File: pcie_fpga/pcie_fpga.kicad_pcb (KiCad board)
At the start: 4 copper layers, 50 x 70 mm, 18 parts, among them J3 Bus_PCI_Express_x4, U1 XC7A50T-FGG484, U2 LTC6957xMS-2, X1 ECS-2520MVQ-1000-BN-TR

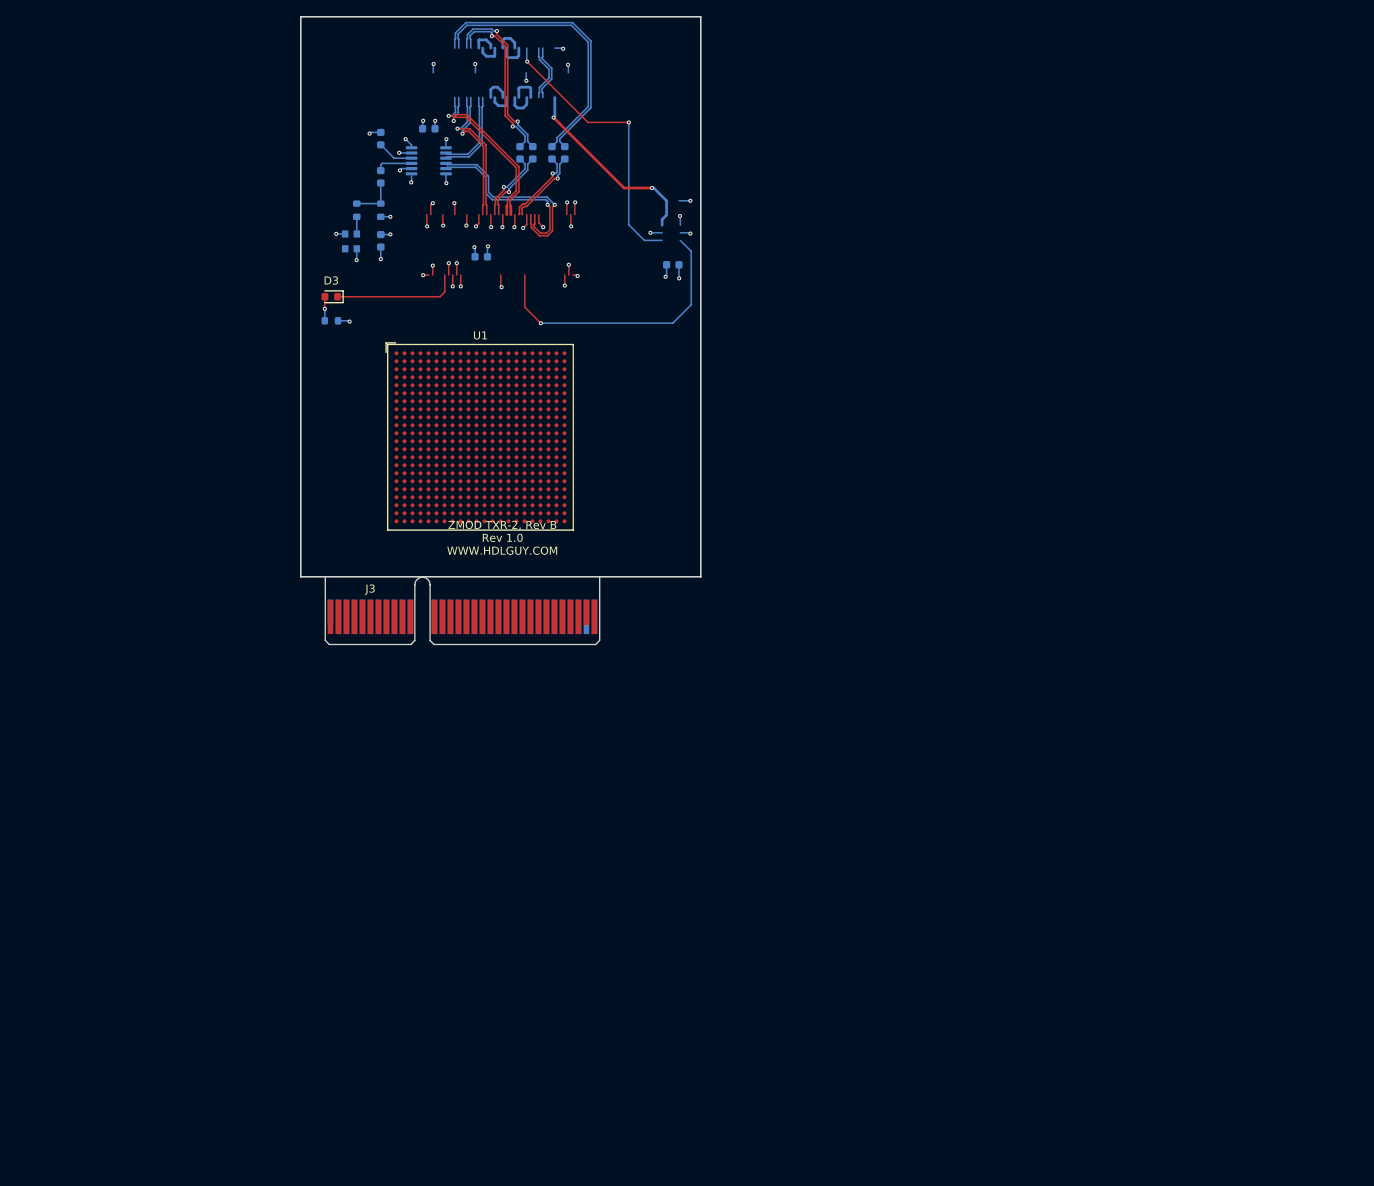
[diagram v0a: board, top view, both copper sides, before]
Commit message: brought in the lucanastasio PCIe board template
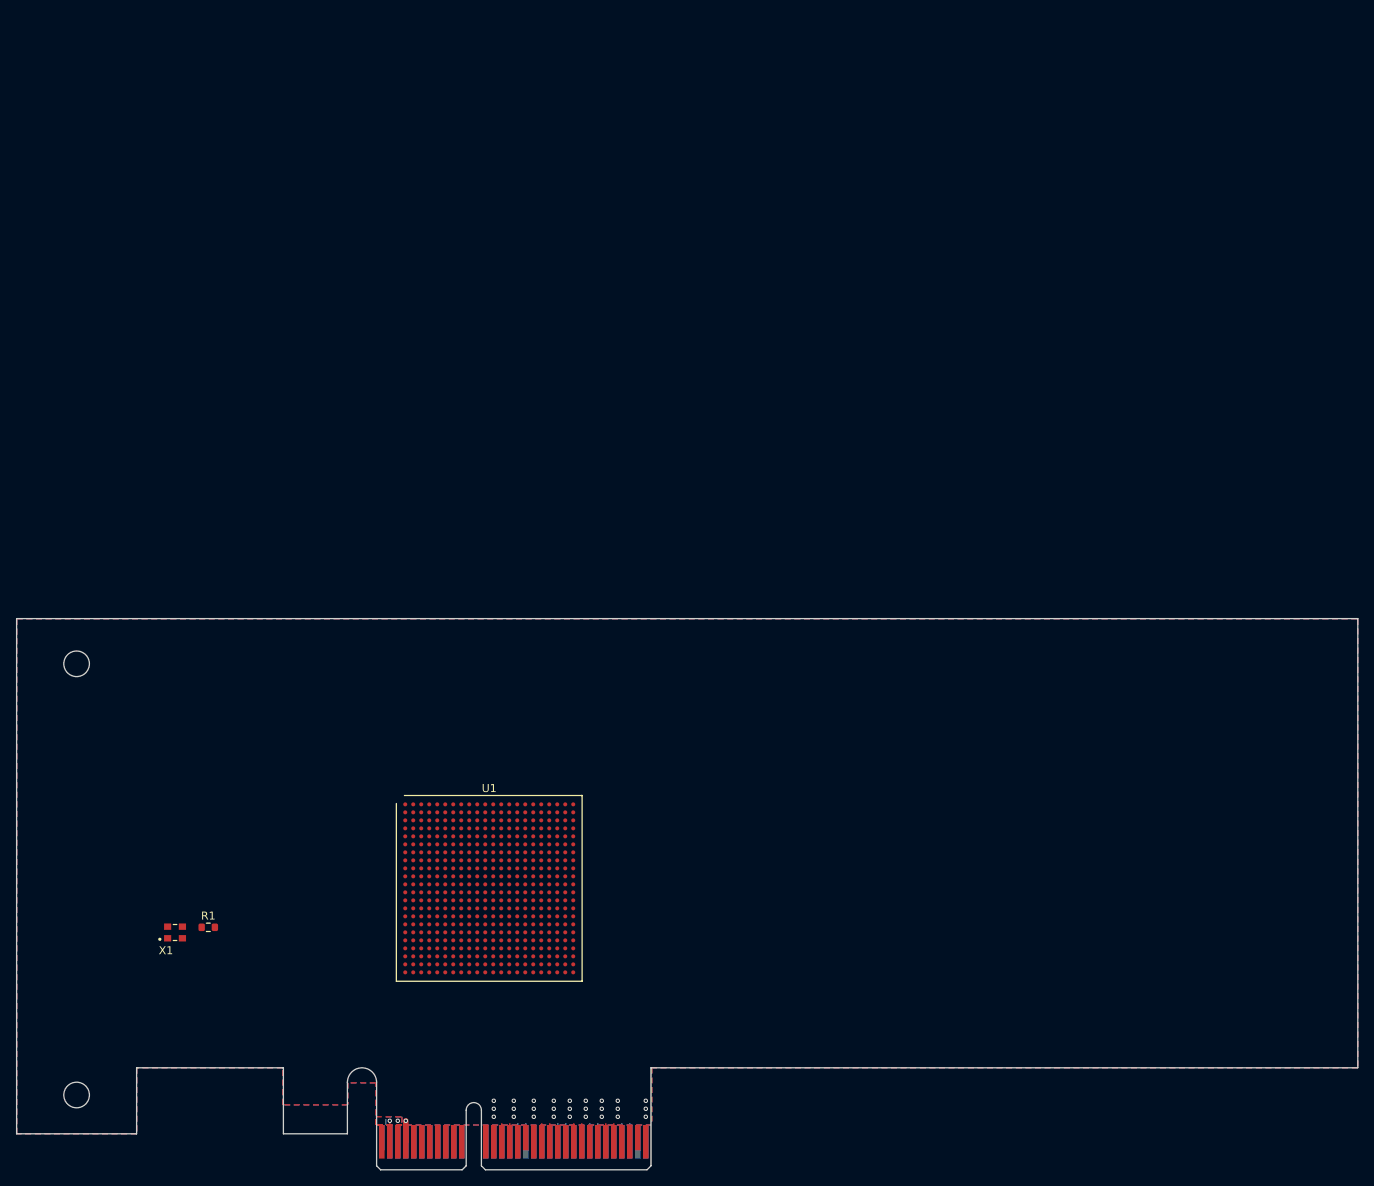
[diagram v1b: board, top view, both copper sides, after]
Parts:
- removed C1, C11, C2, C3, C4, C5, C6, C7, C8, C9: 0.01uf, Capacitor_SMD:C_0603_1608Metric
- removed D3: LED, LED_SMD:LED_0603_1608Metric
- removed J3: Bus_PCI_Express_x4, Connector_PCBEdge:BUS_PCIexpress_x4
- removed R2: 49.9, Resistor_SMD:R_0603_1608Metric
- removed R3: 240, Resistor_SMD:R_0603_1608Metric
- removed U2: LTC6957xMS-2, Package_SO:MSOP-12_3x4mm_P0.65mm
- added J2: PCIexpress_x4, PCIexpress:PCIexpress_x4, F.Cu at (109.6, 194.1)
- R1: value 100 -> 10; moved to F.Cu
- U1: footprint Package_BGA:BGA-484_23.0x23.0mm_Layout22x22_P1.0mm -> Package_BGA:Xilinx_FGG484
- X1: moved to F.Cu
- moved R1 91.5 mm to (88.4, 163.8), turned to 0 degrees
- moved X1 89.1 mm to (84.3, 164.5), turned to 0 degrees
- moved U1 56.4 mm to (123.6, 158.9)
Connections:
- net Net-(R1-Pad2) renamed /oscout
- R1 pad 1: Net-(C6-Pad1) -> /fpga_clk
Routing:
- net (no net): track 215.6 -> 0.00 mm, vias 9 -> 0
- net GND: track 47.2 -> 2.62 mm, vias 34 -> 28
- net /gtr0_tx_P: track 35.4 -> 0.00 mm
- net /gtr0_tx_N: track 34.3 -> 0.00 mm
- net /pcie_refclk_N: track 25.3 -> 0.00 mm, vias 1 -> 0
- net /pcie_refclk_P: track 23.4 -> 0.00 mm, vias 1 -> 0
- net +3V3: track 23.2 -> 0.00 mm, vias 18 -> 0
- net /gtr1_tx_P: track 22.3 -> 0.00 mm, vias 2 -> 0
- net /gtr1_tx_N: track 21.2 -> 0.00 mm, vias 2 -> 0
- net unconnected-(D3-Pad1): track 15.8 -> 0.00 mm
- net /gtrclk0_N: track 11.1 -> 0.00 mm
- net /gtrclk0_P: track 10.5 -> 0.00 mm
- net /gtr0_tx_cc_P: track 9.63 -> 0.00 mm, vias 1 -> 0
- net /gtr0_tx_cc_N: track 9.63 -> 0.00 mm, vias 1 -> 0
- net /gtr1_tx_cc_P: track 9.01 -> 0.00 mm, vias 1 -> 0
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- added copper zone on B.Cu, net +12V
- added copper zone on F.Cu, net +12V
- added copper zone on B.Cu, net GND
- added copper zone on F.Cu, net GND
- added copper zone on In1.Cu, net GND
- removed copper zone on In1.Cu, net +3V3
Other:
- board size 50 x 70 mm -> 167.7 x 68.9 mm
- rule pad_to_mask_clearance: 0 -> 0.051
- board text removed: "ZMOD TXR-2, Rev B Rev 1.0 WWW.HDLGUY.COM"

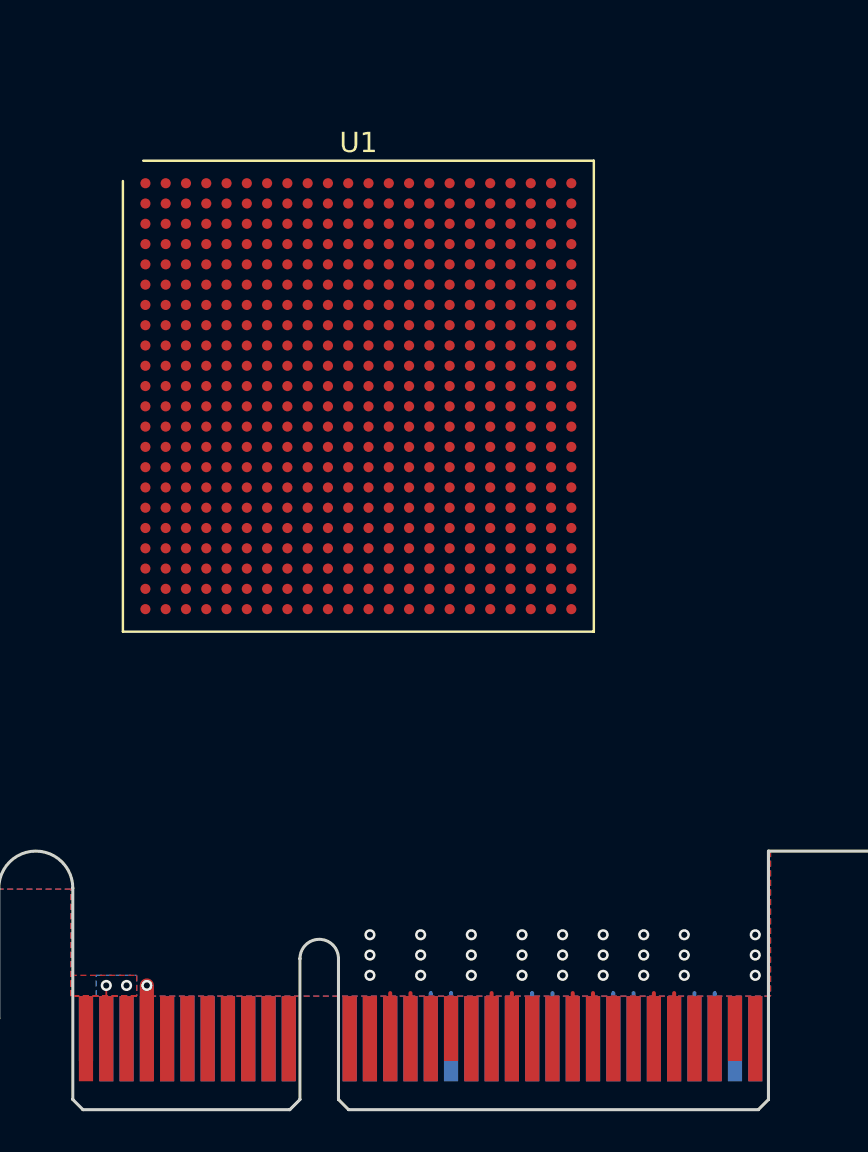
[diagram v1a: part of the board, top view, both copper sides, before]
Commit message: adding more fpga stuff
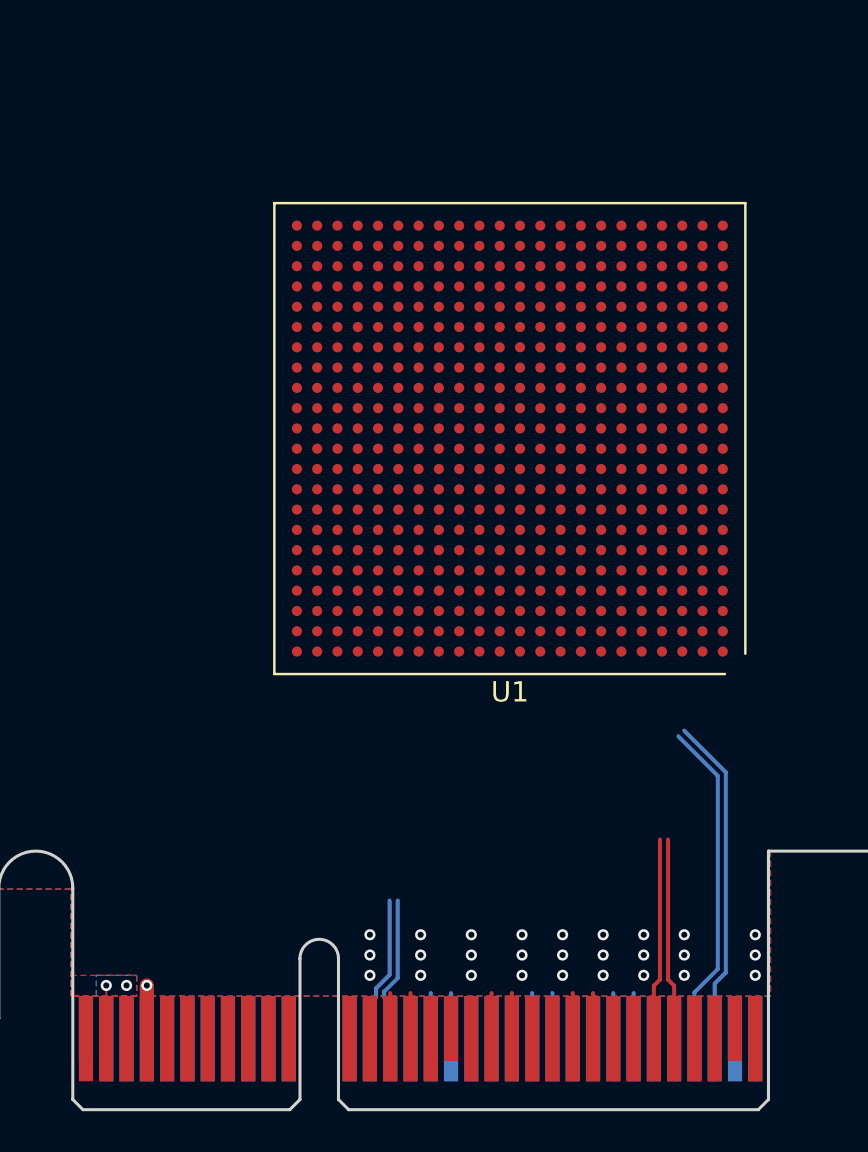
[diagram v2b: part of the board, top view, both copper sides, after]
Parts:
- moved U1 7.76 mm to (131.0, 161.0), turned to 180 degrees
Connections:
- J2 pad A11: unconnected-(J2-PadA11) -> /perstn
- J2 pad A13: unconnected-(J2-PadA13) -> /refclk_P
- J2 pad A14: unconnected-(J2-PadA14) -> /refclk_N
- J2 pad A16: unconnected-(J2-PadA16) -> /per0_P
- J2 pad A17: unconnected-(J2-PadA17) -> /per0_N
- J2 pad A21: unconnected-(J2-PadA21) -> /per1_P
- J2 pad A22: unconnected-(J2-PadA22) -> /per1_N
- J2 pad A25: unconnected-(J2-PadA25) -> /per2_P
- J2 pad A26: unconnected-(J2-PadA26) -> /per2_N
- J2 pad A29: unconnected-(J2-PadA29) -> /per3_P
- J2 pad A30: unconnected-(J2-PadA30) -> /per3_N
- J2 pad B14: unconnected-(J2-PadB14) -> /pet0_P
- J2 pad B15: unconnected-(J2-PadB15) -> /pet0_N
- J2 pad B19: unconnected-(J2-PadB19) -> /pet1_P
- J2 pad B20: unconnected-(J2-PadB20) -> /pet1_N
- J2 pad B23: unconnected-(J2-PadB23) -> /pet2_P
- J2 pad B24: unconnected-(J2-PadB24) -> /pet2_N
- J2 pad B27: unconnected-(J2-PadB27) -> /pet3_P
- J2 pad B28: unconnected-(J2-PadB28) -> /pet3_N
- U1 pad A10: unconnected-(U1-PadA10) -> /pet2_N
- U1 pad A11: unconnected-(U1-PadA11) -> GND
- U1 pad A12: unconnected-(U1-PadA12) -> GND
- U1 pad A2: unconnected-(U1-PadA2) -> GND
- U1 pad A22: unconnected-(U1-PadA22) -> GND
- U1 pad A3: unconnected-(U1-PadA3) -> GND
- U1 pad A4: unconnected-(U1-PadA4) -> /per0_N
- U1 pad A5: unconnected-(U1-PadA5) -> GND
- U1 pad A6: unconnected-(U1-PadA6) -> /per2_N
- U1 pad A7: unconnected-(U1-PadA7) -> GND
- U1 pad A8: unconnected-(U1-PadA8) -> /pet0_N
- U1 pad A9: unconnected-(U1-PadA9) -> GND
- U1 pad AA12: unconnected-(U1-PadAA12) -> GND
- U1 pad AA17: unconnected-(U1-PadAA17) -> +3V3
- U1 pad AA2: unconnected-(U1-PadAA2) -> GND
- U1 pad AA22: unconnected-(U1-PadAA22) -> GND
- U1 pad AB14: unconnected-(U1-PadAB14) -> +3V3
- U1 pad AB19: unconnected-(U1-PadAB19) -> GND
- U1 pad AB9: unconnected-(U1-PadAB9) -> GND
- U1 pad B10: unconnected-(U1-PadB10) -> /pet2_P
- U1 pad B12: unconnected-(U1-PadB12) -> GND
- U1 pad B19: unconnected-(U1-PadB19) -> GND
- U1 pad B3: unconnected-(U1-PadB3) -> GND
- U1 pad B4: unconnected-(U1-PadB4) -> /per0_P
- U1 pad B6: unconnected-(U1-PadB6) -> /per2_P
- U1 pad B8: unconnected-(U1-PadB8) -> /pet0_P
- U1 pad C10: unconnected-(U1-PadC10) -> GND
- U1 pad C11: unconnected-(U1-PadC11) -> /pet1_N
- U1 pad C12: unconnected-(U1-PadC12) -> GND
- U1 pad C16: unconnected-(U1-PadC16) -> GND
- U1 pad C3: unconnected-(U1-PadC3) -> GND
- U1 pad C5: unconnected-(U1-PadC5) -> /per1_N
- U1 pad C6: unconnected-(U1-PadC6) -> GND
- U1 pad C7: unconnected-(U1-PadC7) -> /per3_N
- U1 pad C9: unconnected-(U1-PadC9) -> /pet3_N
- U1 pad D11: unconnected-(U1-PadD11) -> /pet1_P
- U1 pad D12: unconnected-(U1-PadD12) -> GND
- U1 pad D13: unconnected-(U1-PadD13) -> GND
- U1 pad D3: unconnected-(U1-PadD3) -> GND
- U1 pad D4: unconnected-(U1-PadD4) -> GND
- U1 pad D5: unconnected-(U1-PadD5) -> /per1_P
- U1 pad D7: unconnected-(U1-PadD7) -> /per3_P
- U1 pad D8: unconnected-(U1-PadD8) -> GND
- U1 pad D9: unconnected-(U1-PadD9) -> /pet3_P
- U1 pad E11: unconnected-(U1-PadE11) -> GND
- U1 pad E12: unconnected-(U1-PadE12) -> GND
- U1 pad E20: unconnected-(U1-PadE20) -> GND
- U1 pad E4: unconnected-(U1-PadE4) -> GND
- U1 pad E5: unconnected-(U1-PadE5) -> GND
- U1 pad E6: unconnected-(U1-PadE6) -> /refclk_N
- U1 pad E7: unconnected-(U1-PadE7) -> GND
- U1 pad E9: unconnected-(U1-PadE9) -> GND
- U1 pad F11: unconnected-(U1-PadF11) -> GND
- U1 pad F17: unconnected-(U1-PadF17) -> GND
- U1 pad F5: unconnected-(U1-PadF5) -> GND
- U1 pad F6: unconnected-(U1-PadF6) -> /refclk_P
- U1 pad G10: unconnected-(U1-PadG10) -> GND
- U1 pad G12: unconnected-(U1-PadG12) -> GND
- U1 pad G14: unconnected-(U1-PadG14) -> GND
- U1 pad G5: unconnected-(U1-PadG5) -> GND
- U1 pad G6: unconnected-(U1-PadG6) -> GND
- U1 pad G7: unconnected-(U1-PadG7) -> GND
- U1 pad G8: unconnected-(U1-PadG8) -> GND
- U1 pad G9: unconnected-(U1-PadG9) -> GND
- U1 pad H1: unconnected-(U1-PadH1) -> GND
- U1 pad H10: unconnected-(U1-PadH10) -> +1V0
- U1 pad H11: unconnected-(U1-PadH11) -> GND
- U1 pad H12: unconnected-(U1-PadH12) -> +1V8
- U1 pad H21: unconnected-(U1-PadH21) -> GND
- U1 pad H7: unconnected-(U1-PadH7) -> GND
- U1 pad H8: unconnected-(U1-PadH8) -> +1V0
- U1 pad H9: unconnected-(U1-PadH9) -> GND
- U1 pad J10: unconnected-(U1-PadJ10) -> GND
- U1 pad J11: unconnected-(U1-PadJ11) -> +1V0
- U1 pad J12: unconnected-(U1-PadJ12) -> GND
- U1 pad J18: unconnected-(U1-PadJ18) -> GND
- U1 pad J7: unconnected-(U1-PadJ7) -> +1V0
- U1 pad J8: unconnected-(U1-PadJ8) -> GND
- U1 pad J9: unconnected-(U1-PadJ9) -> +1V0
- U1 pad K10: unconnected-(U1-PadK10) -> +1V8
- U1 pad K11: unconnected-(U1-PadK11) -> GND
- U1 pad K12: unconnected-(U1-PadK12) -> +1V8
- U1 pad K15: unconnected-(U1-PadK15) -> GND
- U1 pad K5: unconnected-(U1-PadK5) -> GND
- U1 pad K7: unconnected-(U1-PadK7) -> GND
- U1 pad K8: unconnected-(U1-PadK8) -> +1V0
- U1 pad K9: unconnected-(U1-PadK9) -> GND
- U1 pad L11: unconnected-(U1-PadL11) -> +1V0
- U1 pad L2: unconnected-(U1-PadL2) -> GND
- U1 pad L22: unconnected-(U1-PadL22) -> GND
- U1 pad L7: unconnected-(U1-PadL7) -> +1V0
- U1 pad L8: unconnected-(U1-PadL8) -> GND
- U1 pad M11: unconnected-(U1-PadM11) -> GND
- U1 pad M12: unconnected-(U1-PadM12) -> +1V8
- U1 pad M14: unconnected-(U1-PadM14) -> +3V3
- U1 pad M19: unconnected-(U1-PadM19) -> GND
- U1 pad M7: unconnected-(U1-PadM7) -> GND
- U1 pad M8: unconnected-(U1-PadM8) -> +1V0
- U1 pad N11: unconnected-(U1-PadN11) -> +1V0
- U1 pad N15: unconnected-(U1-PadN15) -> /perstn
- U1 pad N16: unconnected-(U1-PadN16) -> GND
- U1 pad N6: unconnected-(U1-PadN6) -> GND
- U1 pad N7: unconnected-(U1-PadN7) -> +1V0
- U1 pad N8: unconnected-(U1-PadN8) -> GND
- U1 pad P10: unconnected-(U1-PadP10) -> +1V0
- U1 pad P11: unconnected-(U1-PadP11) -> GND
- U1 pad P12: unconnected-(U1-PadP12) -> +1V8
- U1 pad P13: unconnected-(U1-PadP13) -> GND
- U1 pad P18: unconnected-(U1-PadP18) -> +3V3
- U1 pad P3: unconnected-(U1-PadP3) -> GND
- U1 pad P7: unconnected-(U1-PadP7) -> GND
- U1 pad P8: unconnected-(U1-PadP8) -> +1V0
- U1 pad P9: unconnected-(U1-PadP9) -> GND
- U1 pad R10: unconnected-(U1-PadR10) -> GND
- U1 pad R11: unconnected-(U1-PadR11) -> +1V8
- U1 pad R12: unconnected-(U1-PadR12) -> GND
- U1 pad R15: unconnected-(U1-PadR15) -> +3V3
- U1 pad R20: unconnected-(U1-PadR20) -> GND
- U1 pad R7: unconnected-(U1-PadR7) -> +1V0
- U1 pad R8: unconnected-(U1-PadR8) -> GND
- U1 pad R9: unconnected-(U1-PadR9) -> +1V0
- U1 pad T10: unconnected-(U1-PadT10) -> +1V0
- U1 pad T11: unconnected-(U1-PadT11) -> GND
- U1 pad T17: unconnected-(U1-PadT17) -> GND
- U1 pad T22: unconnected-(U1-PadT22) -> +3V3
- U1 pad T7: unconnected-(U1-PadT7) -> GND
- U1 pad T8: unconnected-(U1-PadT8) -> +1V0
- U1 pad T9: unconnected-(U1-PadT9) -> GND
- U1 pad U14: unconnected-(U1-PadU14) -> GND
- U1 pad U19: unconnected-(U1-PadU19) -> +3V3
- U1 pad U4: unconnected-(U1-PadU4) -> GND
- U1 pad V1: unconnected-(U1-PadV1) -> GND
- U1 pad V11: unconnected-(U1-PadV11) -> GND
- U1 pad V16: unconnected-(U1-PadV16) -> +3V3
- U1 pad V21: unconnected-(U1-PadV21) -> GND
- U1 pad W13: unconnected-(U1-PadW13) -> +3V3
- U1 pad W18: unconnected-(U1-PadW18) -> GND
- U1 pad W19: unconnected-(U1-PadW19) -> /fpga_clk
- U1 pad W8: unconnected-(U1-PadW8) -> GND
- U1 pad Y10: unconnected-(U1-PadY10) -> +3V3
- U1 pad Y15: unconnected-(U1-PadY15) -> GND
- U1 pad Y20: unconnected-(U1-PadY20) -> +3V3
- U1 pad Y5: unconnected-(U1-PadY5) -> GND
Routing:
- net /per3_N: track 0.00 -> 16.3 mm
- net /per3_P: track 0.00 -> 16.2 mm
- net /pet3_P: track 0.00 -> 9.94 mm
- net /pet3_N: track 0.00 -> 9.94 mm
- net /refclk_P: track 0.00 -> 7.21 mm
- net /refclk_N: track 0.00 -> 7.21 mm
- net unconnected-(J2-PadB28): track 2.25 -> 0.00 mm
- net unconnected-(J2-PadB27): track 2.25 -> 0.00 mm
- net unconnected-(J2-PadB24): track 2.25 -> 0.00 mm
- net unconnected-(J2-PadB23): track 2.25 -> 0.00 mm
- net unconnected-(J2-PadB20): track 2.25 -> 0.00 mm
- net unconnected-(J2-PadB19): track 2.25 -> 0.00 mm
- net unconnected-(J2-PadB15): track 2.25 -> 0.00 mm
- net unconnected-(J2-PadB14): track 2.25 -> 0.00 mm
- net unconnected-(J2-PadA30): track 2.25 -> 0.00 mm
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
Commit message: tweaks, thinking about it some more
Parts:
- moved U1 7.55 mm to (123.9, 158.4)
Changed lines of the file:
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@@
   )
   (footprint "Package_BGA:Xilinx_FGG484" (layer "F.Cu")
-    (at 131.025 161.035 180)
+    (at 123.945 158.425 180)
     (descr "Artix-7 BGA, 22x22 grid, 23x23mm package, 1mm pitch; https://www.xilinx.com/support/documentation/user_guides/ug475_7Series_Pkg_Pinout.pdf#page=275, NSMD pad definition Appendix A")
     (tags "BGA 484 1 FG484 FGG484")
